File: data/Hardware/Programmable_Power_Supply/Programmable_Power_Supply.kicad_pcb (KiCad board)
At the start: 4 copper layers, 119 x 74 mm, 84 parts, among them J1 Barrel Jack Input Port, J2 Phoenix Contact 1891519, J4 SWD Debugging Port, J5 Two Pin Fan Header, J6 USB_C_Receptacle_USB2.0_16P, Q1 BSC050N03LS_G, Q2 2N7002, Q3 BSC050N03LS_G, Q4 BSC050N03LS_G, Q5 2N7002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

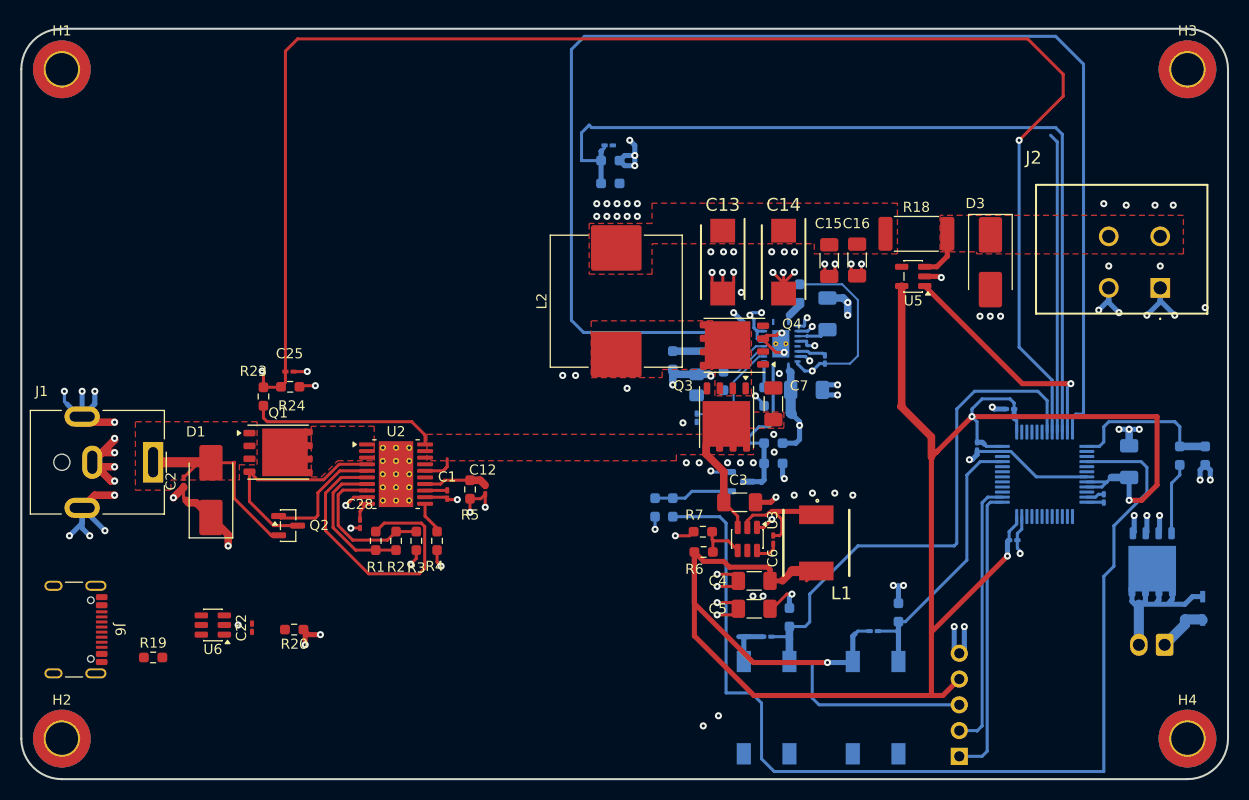
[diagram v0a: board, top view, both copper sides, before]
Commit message: feat: Layout of USB-C port and final beta version of the board.
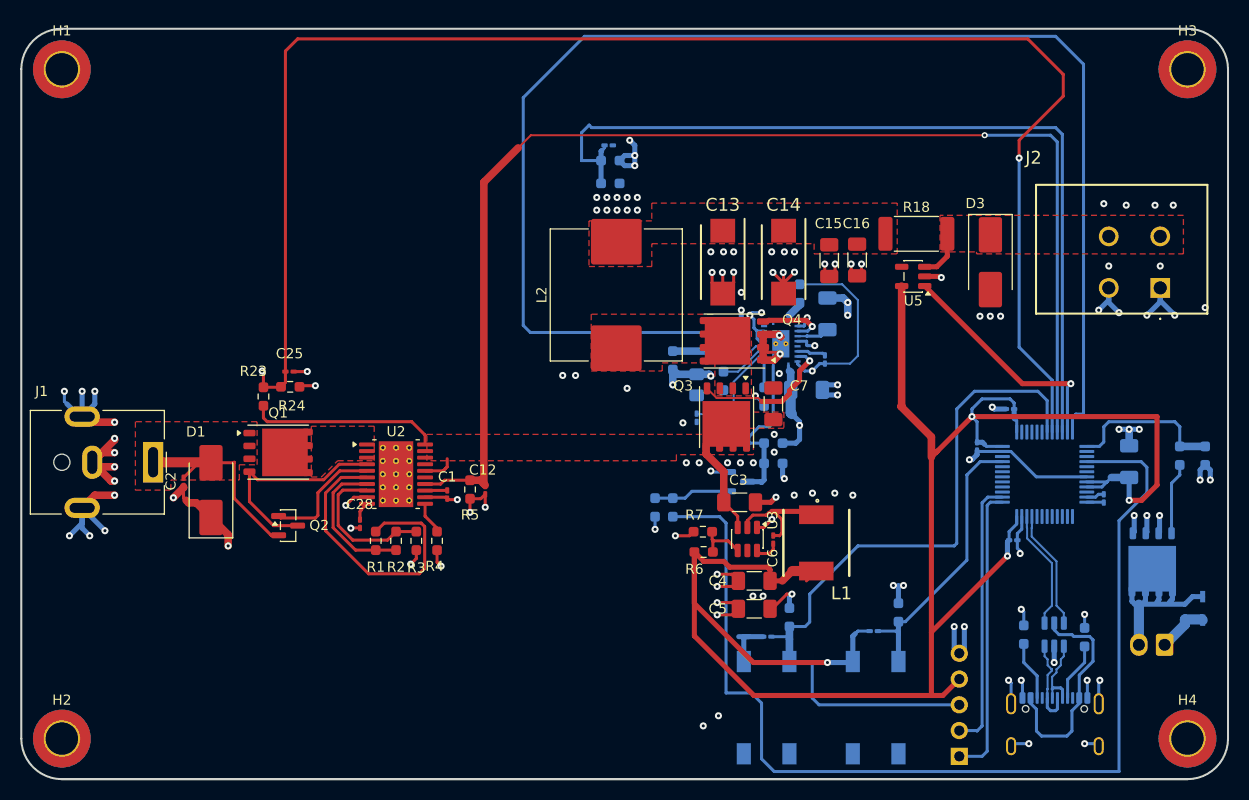
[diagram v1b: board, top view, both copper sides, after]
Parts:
- removed C22: 100n, Capacitor_SMD:C_0201_0603Metric_Pad0.64x0.40mm_HandSolder
- J6, R19, R20, U6: moved to B.Cu
- moved J6 98.2 mm to (236.9, 104.7), turned to 180 degrees
- moved R19 91.9 mm to (239.9, 95.0), turned to -90 degrees
- moved U6 83.0 mm to (236.9, 94.8), turned to 90 degrees
- moved R20 71.9 mm to (233.9, 94.8), turned to -90 degrees
- moved L2 0.62 mm to (193.7, 61.2)
- moved Q4 0.42 mm to (205.3, 65.8)
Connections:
- net Net-(U6-VBUS) renamed /USB_5V
- J6 pad A6: /USB_D+_RAW -> /USB_RAW_D+
- J6 pad A7: /USB_D-_RAW -> /USB_RAW_D-
- J6 pad B6: /USB_D+_RAW -> /USB_RAW_D+
- J6 pad B7: /USB_D-_RAW -> /USB_RAW_D-
- U6 pad 1: /USB_D+_RAW -> /USB_RAW_D-
- U6 pad 3: /USB_D-_RAW -> /USB_RAW_D+
- U6 pad 4: /USB_D- -> /USB_D+
- U6 pad 6: /USB_D+ -> /USB_D-
- U7 pad V: (no net) -> GND
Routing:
- net /IMON_IN: track 35.8 -> 123.4 mm, vias 0 -> 1
- net /USB_5V: track 0.00 -> 22.2 mm
- net GND: track 200.9 -> 219.7 mm, vias 129 -> 135
- net /Output Section/LM_HO: track 1.38 -> 14.4 mm
- net /USB_D-: track 0.00 -> 11.8 mm
- net /USB_D+: track 0.00 -> 11.8 mm
- net /USB_RAW_D+: track 0.00 -> 8.84 mm
- net /USB_RAW_D-: track 0.00 -> 7.58 mm
- net /FB_OUT: track 131.5 -> 138.6 mm
- net Net-(J6-CC2): track 0.00 -> 5.88 mm
- net Net-(J6-CC1): track 0.00 -> 5.78 mm
- net /Output Section/LM_LO: track 1.64 -> 6.79 mm
- net /EN_OUT: track 103.9 -> 104.7 mm
- added copper zone on In1.Cu, net GND
- added copper zone on In2.Cu, net GND
